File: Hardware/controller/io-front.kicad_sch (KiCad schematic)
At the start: 20 parts

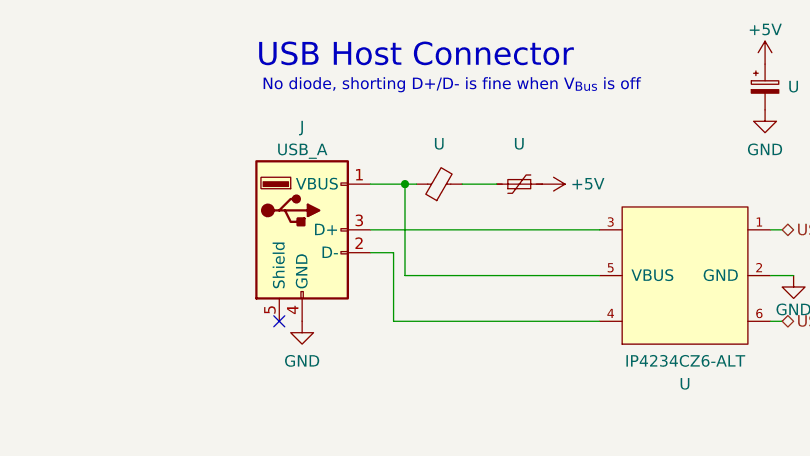
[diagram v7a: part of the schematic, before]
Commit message: ERC and manufacturability tweaks for controller
- Fixed issues that prevented successful ERC runs from happening

- Tweaked a few routing/traces, mostly to increase some clearances and
  spacings

- Added an LM75-style ambient temperature sensor
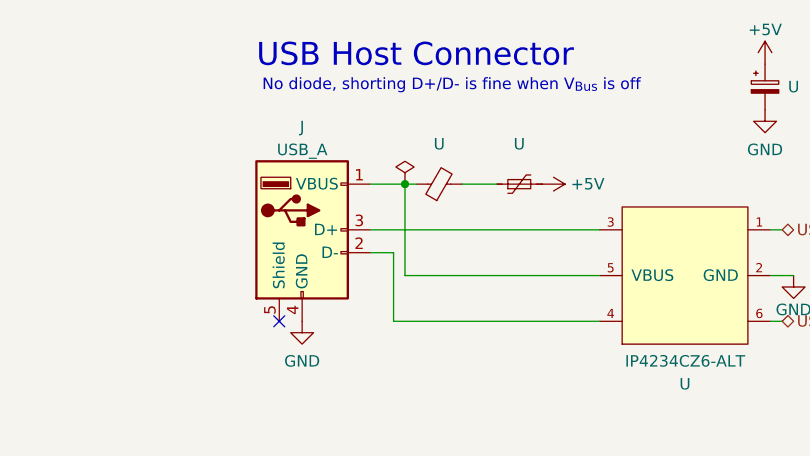
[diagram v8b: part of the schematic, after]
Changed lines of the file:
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@@
+    (pin "1")
+  )
+  (symbol (lib_id "power:PWR_FLAG") (at 143.51 31.75 0) (unit 1)
+    (in_bom yes) (on_board yes) (fields_autoplaced)
+    (default_instance (reference "#FLG") (unit 1) (value "PWR_FLAG") (footprint ""))
+    (property "Reference" "#FLG" (id 0) (at 143.51 29.845 0)
+      (effects (font (size 1.27 1.27)) hide)
+    )
+    (property "Value" "PWR_FLAG" (id 1) (at 143.51 27.94 0)
+      (effects (font (size 1.27 1.27)) hide)
+    )
+    (property "Footprint" "" (id 2) (at 143.51 31.75 0)
+      (effects (font (size 1.27 1.27)) hide)
+    )
+    (property "Datasheet" "~" (id 3) (at 143.51 31.75 0)
+      (effects (font (size 1.27 1.27)) hide)
+    )
     (pin "1")
   )
